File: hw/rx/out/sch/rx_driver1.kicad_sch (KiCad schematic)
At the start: 32 parts, among them K1 TQ2SA-12V, U6 OPA1656

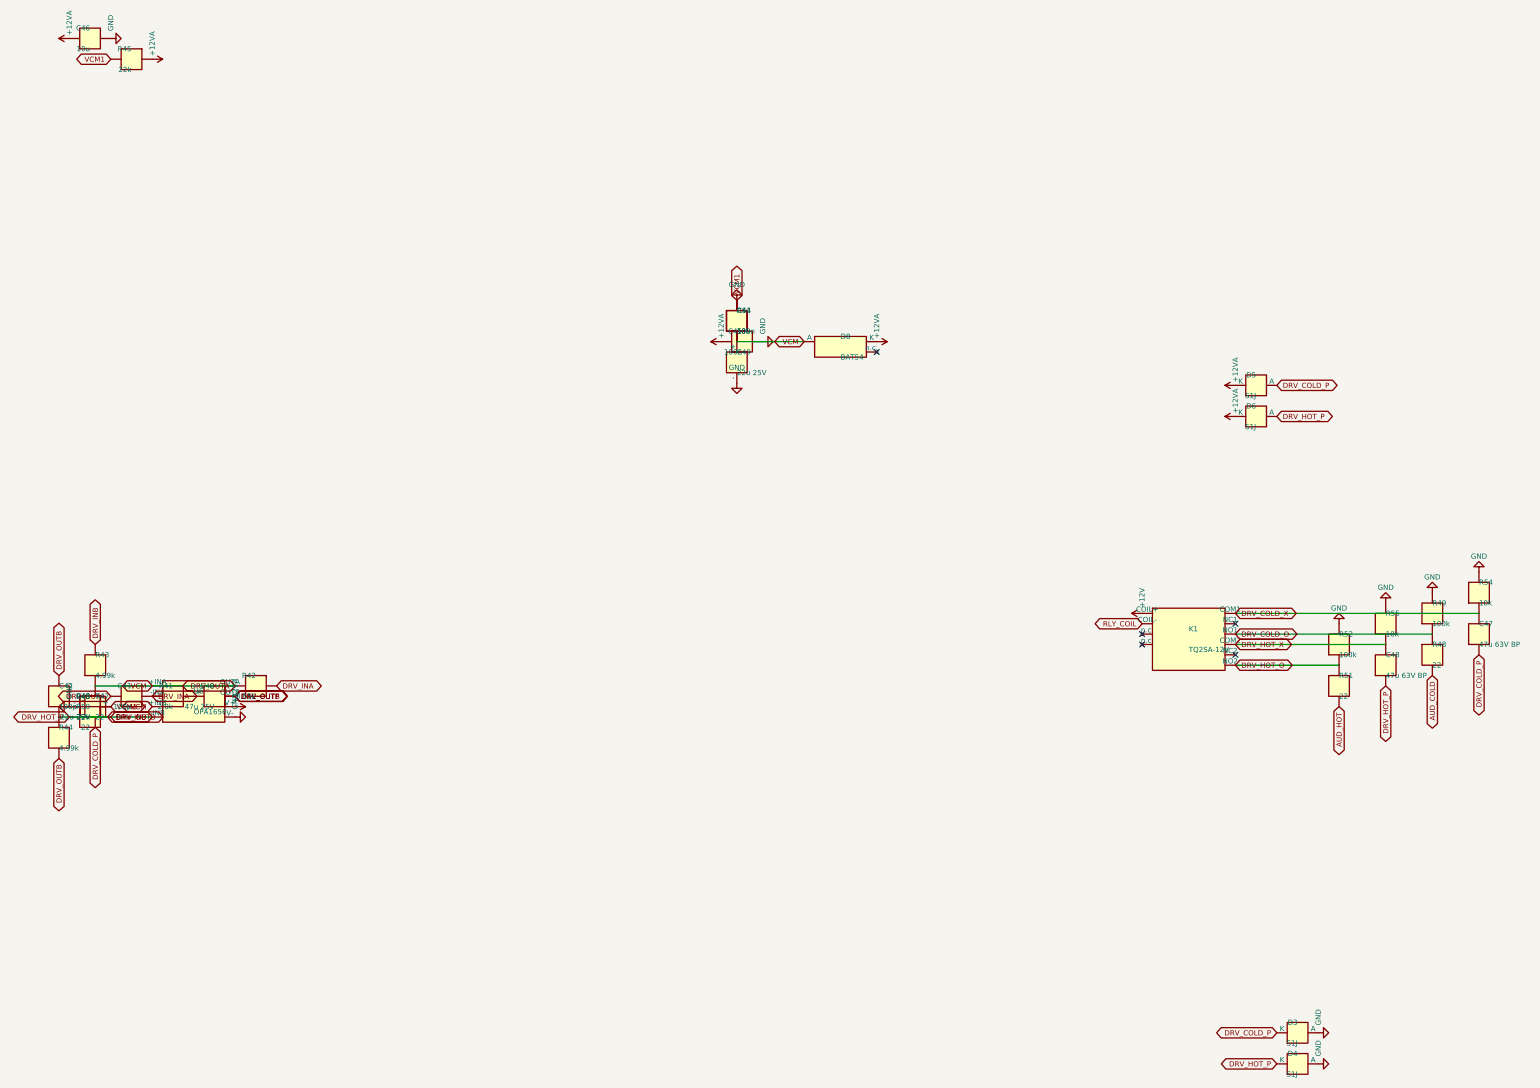
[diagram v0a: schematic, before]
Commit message: hw/rx: BT40E + TQ2SA footprints, THT underside backplane header, bring-up test points (#34)
Co-Authored-By: Claude Opus 5.5 <noreply@anthropic.com>
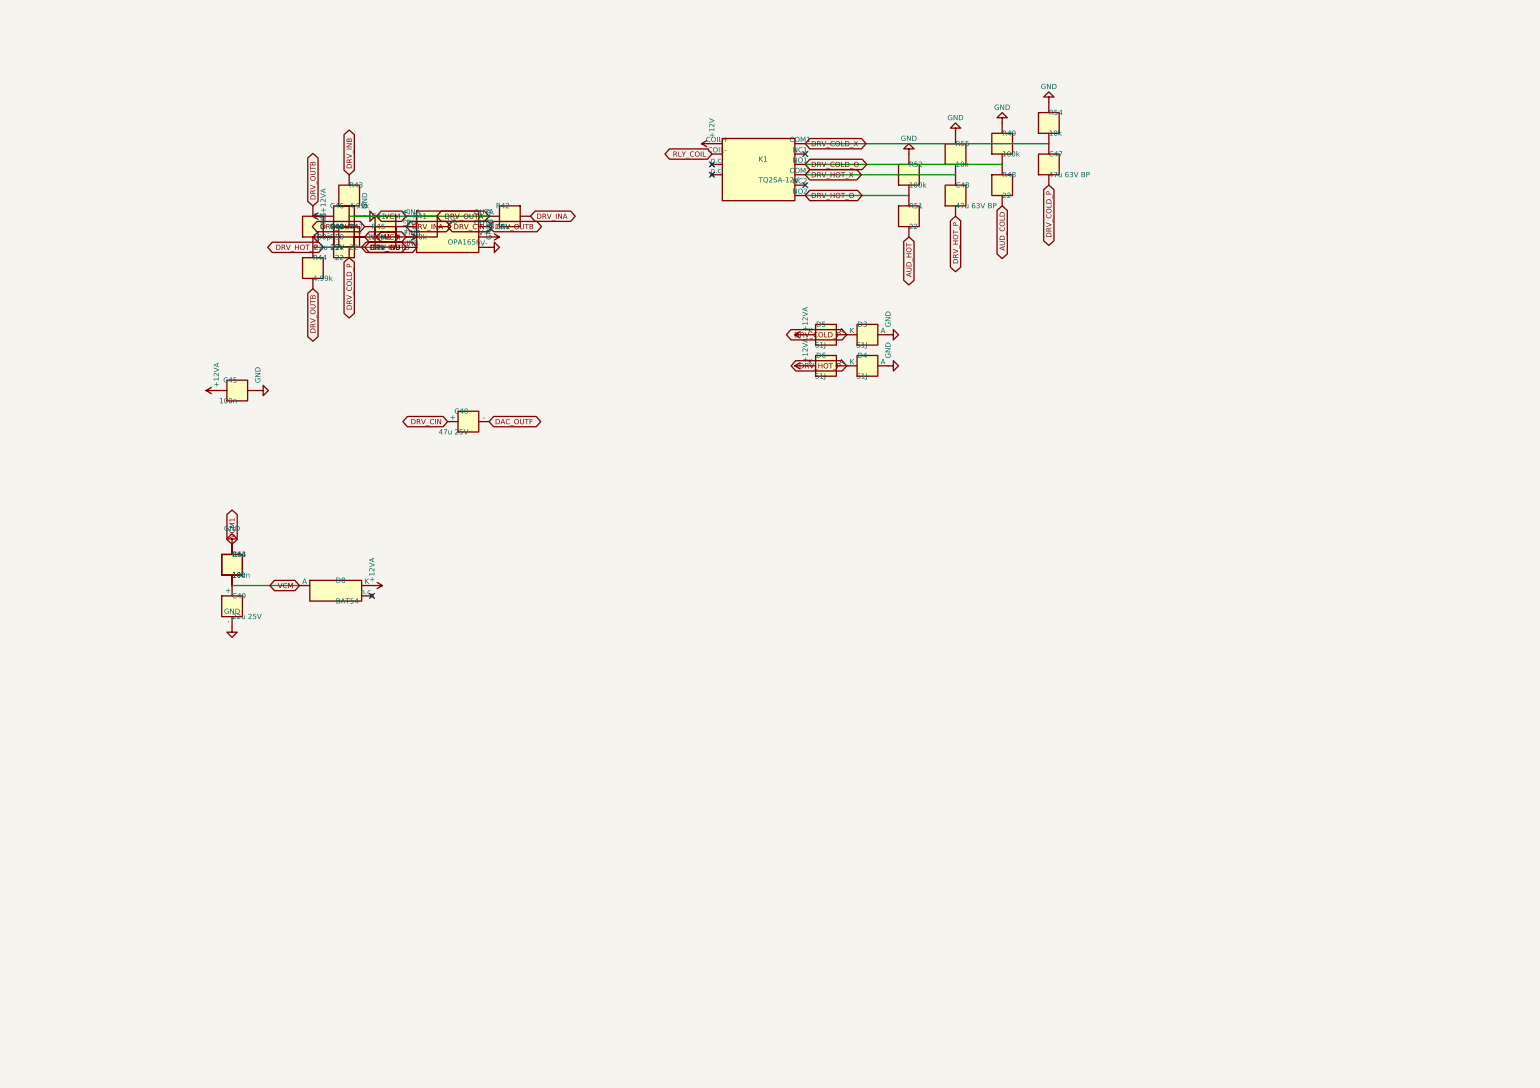
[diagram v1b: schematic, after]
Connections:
- net DRV_OUTA is gone; now on net +12VA: C41.2, C44.1, C49.1 (+), D8.1 (A), R42.2, R43.1, R47.1, R53.2, U6.1 (OUTA), U6.3 (+INA), U6.5 (+INB)
- net DAC_OUTF: no longer C42.1, C42.2, C48.1, D4.1 (K), D6.2 (A), R43.2, R44.1, R44.2, R50.1, R50.2, U6.6 (-INB), U6.7 (OUTB)
- net DRV_CIN: now reaches C40.1 (+), R41.1
- new net DRV_HOT_P: C42.1, C42.2, C48.1, D4.1 (K), D6.2 (A), R43.2, R44.1, R44.2, R50.1, R50.2, U6.6 (-INB), U6.7 (OUTB)
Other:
- moved on the sheet: C40, C41, C42, C43, C44, C45, C46, C47, C48, C49, D3, D4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
